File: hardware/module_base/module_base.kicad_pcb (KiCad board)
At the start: 2 copper layers, 100 x 100 mm, 26 parts, among them J1 RJ45_LED_Shielded, J2 Conn_01x24_Female, J3 Conn_01x24_Female, J4 Conn_01x06_Male, Q1 Q_NMOS_GSD, Q2 Q_NMOS_GSD, Q3 Q_NMOS_GSD, Q4 Q_NMOS_GSD, Q5 Q_NMOS_GSD, Q6 Q_NMOS_GSD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

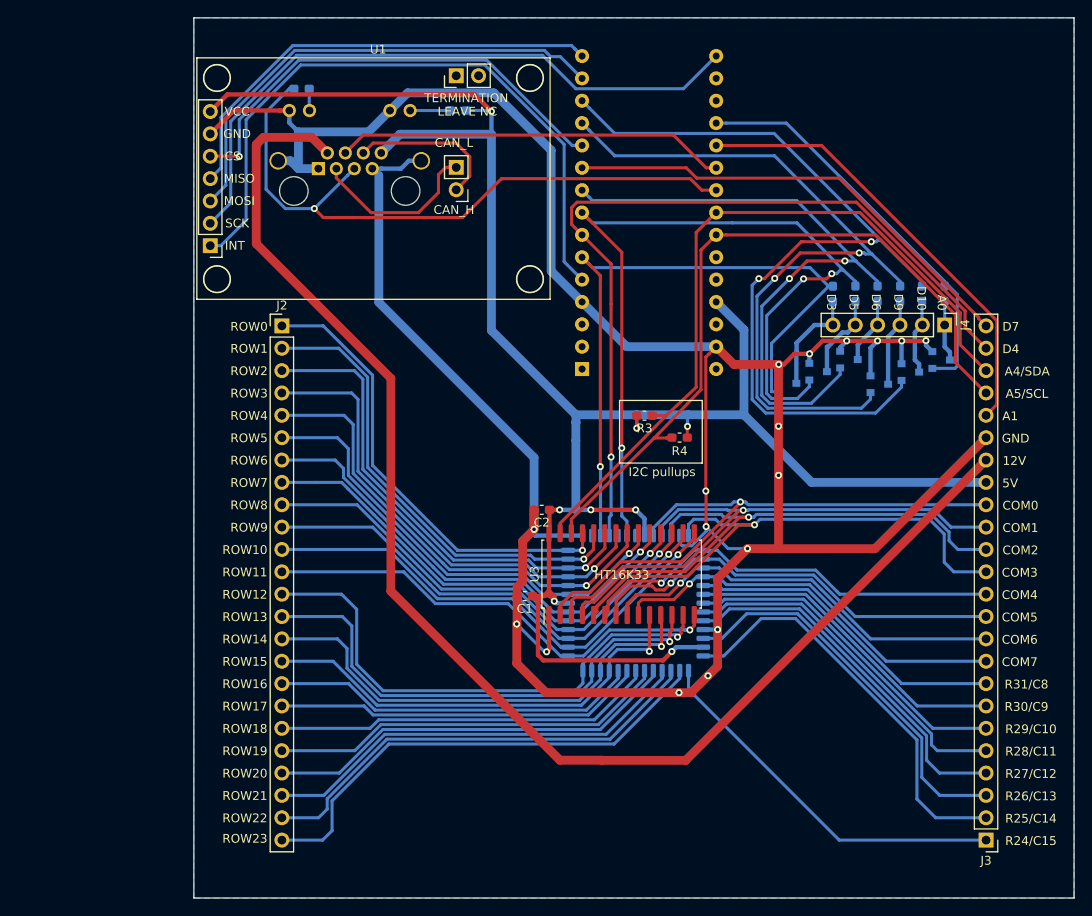
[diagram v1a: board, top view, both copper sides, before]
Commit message: Redo prototyping module layout: CAN module on back, two rows of pins
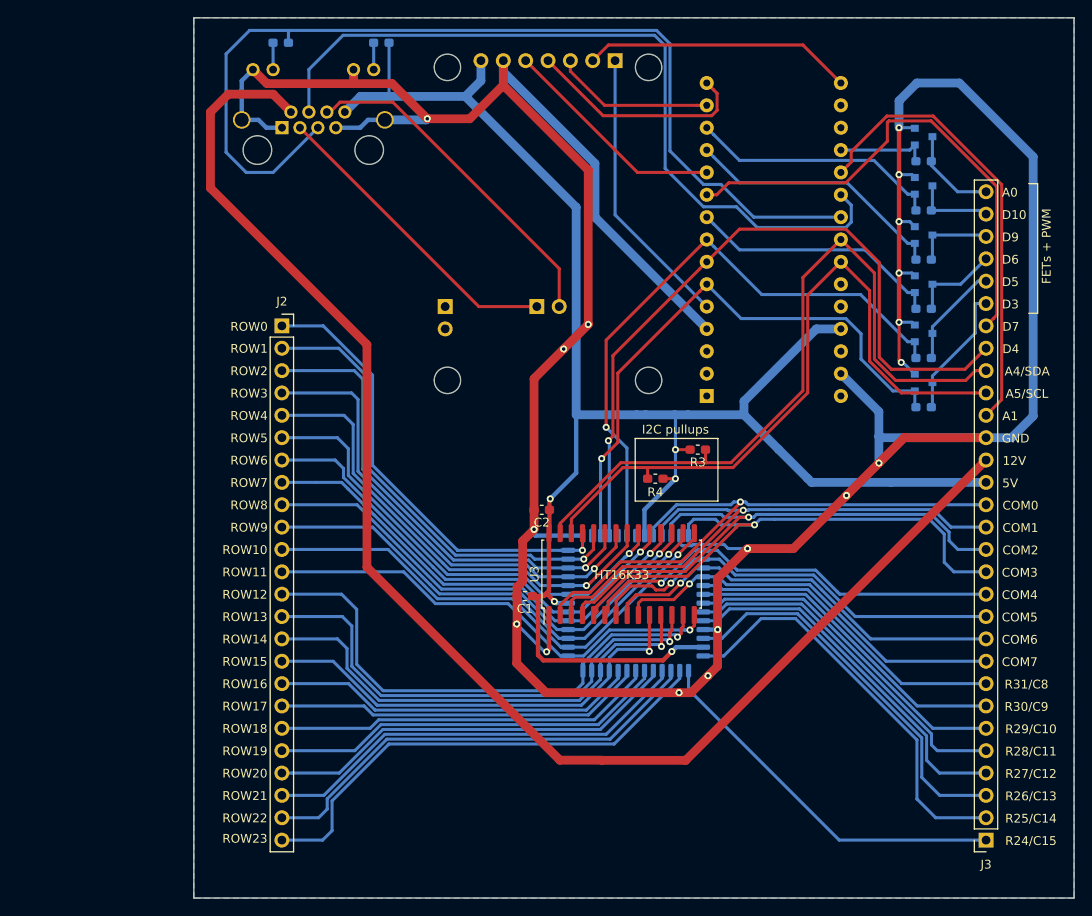
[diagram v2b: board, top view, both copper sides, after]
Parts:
- removed J4: Conn_01x06_Male, Connector_PinHeader_2.54mm:PinHeader_1x06_P2.54mm_Vertical
- J2: footprint Connector_PinHeader_2.54mm:PinHeader_1x24_P2.54mm_Vertical -> Connector_PinSocket_2.54mm:PinSocket_1x24_P2.54mm_Vertical
- J3: value Conn_01x24_Female -> Conn_01x30_Female; footprint Connector_PinHeader_2.54mm:PinHeader_1x24_P2.54mm_Vertical -> Connector_PinSocket_2.54mm:PinSocket_1x30_P2.54mm_Vertical
- U1: moved to B.Cu
- moved Q6 32.0 mm to (152.9, 63.5)
- moved Q5 24.3 mm to (152.9, 69.1)
- moved R10 18.3 mm to (152.9, 66.3), turned to 180 degrees
- moved U1 17.7 mm to (93.5, 63.5), turned to 270 degrees
- moved Q4 16.5 mm to (152.9, 74.7)
- moved A1 14.5 mm to (128.3, 93.0)
- moved R5 13.1 mm to (152.9, 94.2), turned to 180 degrees
- moved Q3 12.4 mm to (152.9, 80.3)
- moved R9 12.2 mm to (152.9, 71.9), turned to 180 degrees
- moved R1 11.6 mm to (91.3, 52.8)
- moved R6 7.30 mm to (152.9, 88.6), turned to 180 degrees
- moved R3 7.18 mm to (127.3, 99.1)
- moved R8 6.51 mm to (152.9, 77.5), turned to 180 degrees
- moved J1 6.22 mm to (80.0, 62.5)
- moved R2 5.74 mm to (79.9, 52.8), turned to 0 degrees
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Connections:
- Q1 pad 1: A0 -> D3
- Q1 pad 3: Net-(J4-Pad1) -> Net-(J3-Pad25)
- Q2 pad 1: D10 -> D5
- Q2 pad 3: Net-(J4-Pad2) -> Net-(J3-Pad26)
- Q3 pad 1: D9 -> D6
- Q3 pad 3: Net-(J4-Pad3) -> Net-(J3-Pad27)
- Q4 pad 1: D6 -> D9
- Q4 pad 3: Net-(J4-Pad4) -> Net-(J3-Pad28)
- Q5 pad 1: D5 -> D10
- Q5 pad 3: Net-(J4-Pad5) -> Net-(J3-Pad29)
- Q6 pad 1: D3 -> A0
- Q6 pad 3: Net-(J4-Pad6) -> Net-(J3-Pad30)
- R10 pad 1: Net-(J4-Pad6) -> Net-(J3-Pad30)
- R10 pad 2: D3 -> A0
- R5 pad 1: Net-(J4-Pad1) -> Net-(J3-Pad25)
- R5 pad 2: A0 -> D3
- R6 pad 1: Net-(J4-Pad2) -> Net-(J3-Pad26)
- R6 pad 2: D10 -> D5
- R7 pad 1: Net-(J4-Pad3) -> Net-(J3-Pad27)
- R7 pad 2: D9 -> D6
- R8 pad 1: Net-(J4-Pad4) -> Net-(J3-Pad28)
- R8 pad 2: D6 -> D9
- R9 pad 1: Net-(J4-Pad5) -> Net-(J3-Pad29)
- R9 pad 2: D5 -> D10
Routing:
- net D10: track 97.0 -> 28.7 mm, vias 2 -> 0
- net D9: track 85.3 -> 29.9 mm, vias 2 -> 0
- net GND: track 344.3 -> 391.1 mm, vias 17 -> 18
- net MODULE_READY: track 44.5 -> 89.1 mm
- net D6: track 72.8 -> 29.1 mm, vias 2 -> 0
- net SCK: track 73.9 -> 30.7 mm
- net Net-(A1-Pad5): track 75.4 -> 32.3 mm
- net MODULE_ENABLE: track 74.3 -> 113.0 mm, vias 1 -> 0
- net MOSI: track 55.0 -> 18.3 mm
- net A0: track 46.8 -> 10.5 mm
- net D5: track 99.7 -> 69.7 mm, vias 3 -> 1
- net Net-(A1-Pad11): track 53.3 -> 25.8 mm, vias 1 -> 0
- net MISO: track 52.3 -> 25.6 mm
- net VCC: track 227.5 -> 204.8 mm, vias 8 -> 5
- net Net-(J1-Pad6): track 17.6 -> 39.0 mm
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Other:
- board text added: "FETs + PWM"

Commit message: ModuleBase PCB: change RJ45 jack, add mounting holes, reorganize
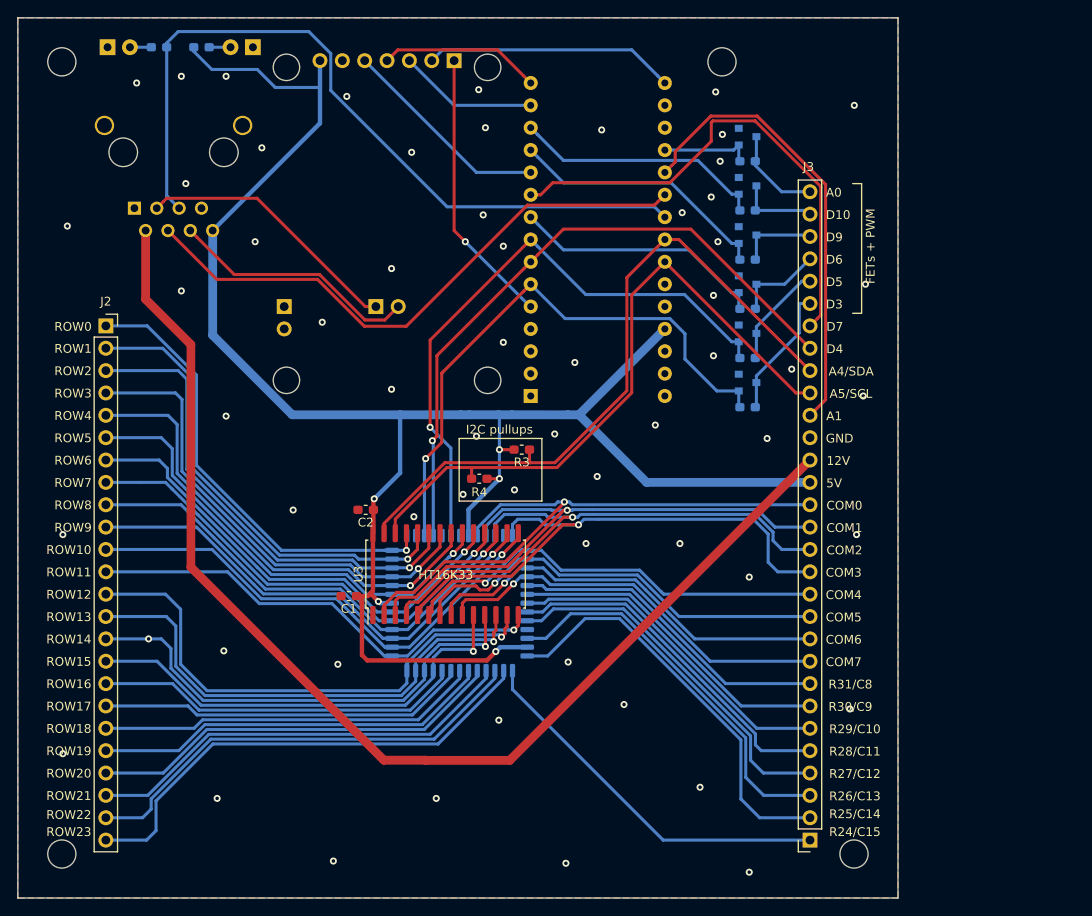
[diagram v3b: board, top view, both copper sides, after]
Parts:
- added D1: LED_Small, LED_THT:LED_D3.0mm, B.Cu at (76.7, 53.3)
- added D2: LED_Small, LED_THT:LED_D3.0mm, B.Cu at (60.2, 53.3)
- added REF**: MountingHole_3.2mm_M3, MountingHole:MountingHole_3.2mm_M3, F.Cu at (55.0, 145.0)
- added REF**: MountingHole_3.2mm_M3, MountingHole:MountingHole_3.2mm_M3, F.Cu at (145.0, 145.0)
- added REF**: MountingHole_3.2mm_M3, MountingHole:MountingHole_3.2mm_M3, F.Cu at (130.0, 55.0)
- added REF**: MountingHole_3.2mm_M3, MountingHole:MountingHole_3.2mm_M3, F.Cu at (55.0, 55.0)
- J1: value RJ45_LED_Shielded -> RJ45_Shielded; footprint Connector_RJ:RJ45_Amphenol_RJHSE538X -> RJ45_5224:RJ45_5224
- moved R1 20.4 mm to (70.9, 53.3), turned to 0 degrees
- moved A1 20.0 mm to (108.3, 93.0)
- moved C1 20.0 mm to (87.6, 115.7)
- moved C2 20.0 mm to (89.5, 105.9)
- moved J2 20.0 mm to (60.0, 85.0)
- moved J3 20.0 mm to (140.0, 143.4)
- moved Q1 20.0 mm to (132.9, 91.4)
- moved Q2 20.0 mm to (132.9, 85.9)
- moved Q3 20.0 mm to (132.9, 80.3)
- moved Q4 20.0 mm to (132.9, 74.7)
- moved Q5 20.0 mm to (132.9, 69.1)
- moved Q6 20.0 mm to (132.9, 63.5)
- moved R10 20.0 mm to (132.9, 66.3)
- moved R3 20.0 mm to (107.3, 99.1)
- moved R4 20.0 mm to (102.4, 102.4)
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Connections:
- R1 pad 2: Net-(J1-Pad12) -> Net-(D1-Pad2)
- R2 pad 1: Net-(J1-Pad10) -> Net-(D2-Pad2)
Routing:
- net GND: track 391.1 -> 0.00 mm, vias 18 -> 60
- net +12V: track 163.5 -> 133.9 mm
- net MODULE_ENABLE: track 113.0 -> 87.7 mm
- net MODULE_READY: track 89.1 -> 67.2 mm
- net Net-(J1-Pad6): track 39.0 -> 28.5 mm
- net VCC: track 204.8 -> 213.7 mm
- net D4: track 82.9 -> 74.6 mm
- net MISO: track 25.6 -> 18.4 mm
- net A4_SDA: track 84.7 -> 78.1 mm
- net Net-(J1-Pad3): track 35.3 -> 30.5 mm
- net A5_SCL: track 79.5 -> 74.8 mm
- net Net-(J1-Pad12): track 3.05 -> 0.00 mm
- net Net-(J1-Pad10): track 3.05 -> 0.00 mm
- net Net-(D2-Pad2): track 0.00 -> 2.43 mm
- net Net-(D1-Pad2): track 0.00 -> 2.43 mm
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- added copper zone on F.Cu, net GND
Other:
- board text added: "Choose FET or resistor for each pin"

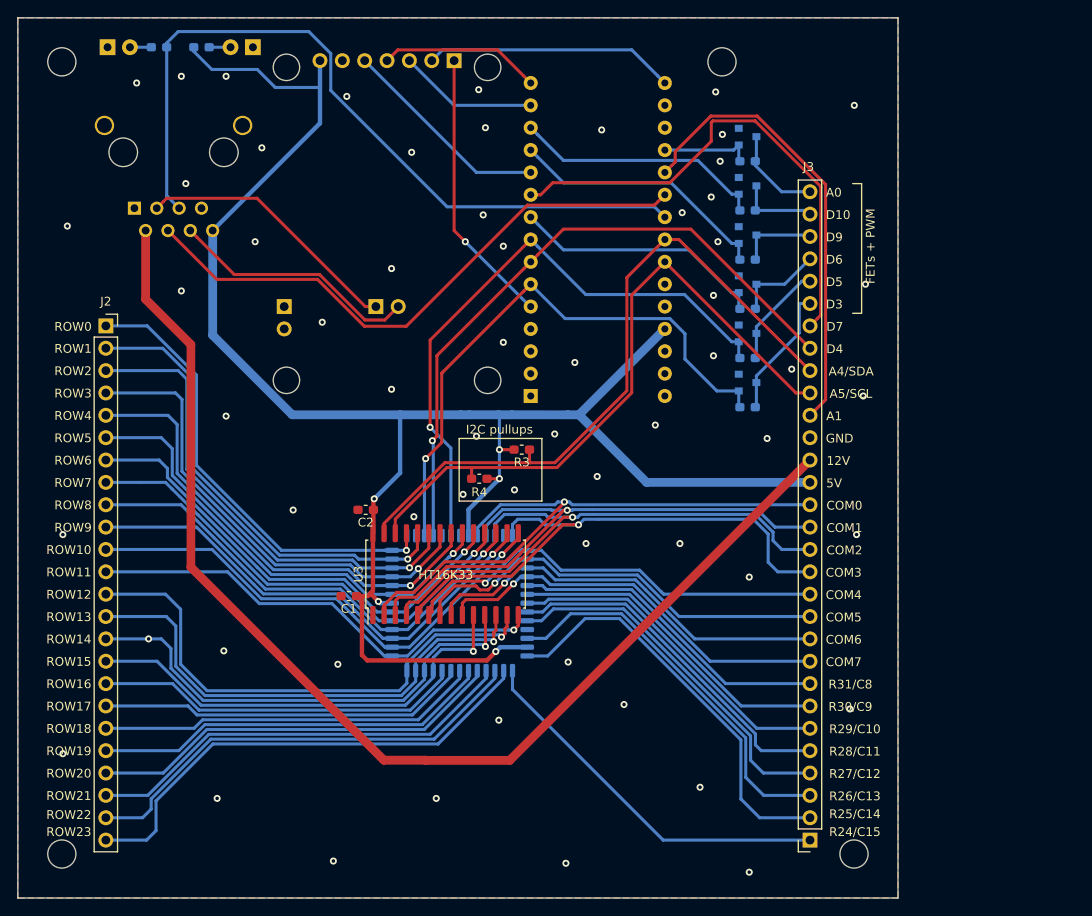
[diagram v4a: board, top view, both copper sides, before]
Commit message: Add identifying silkscreen text, fix missing connections on ModuleBase
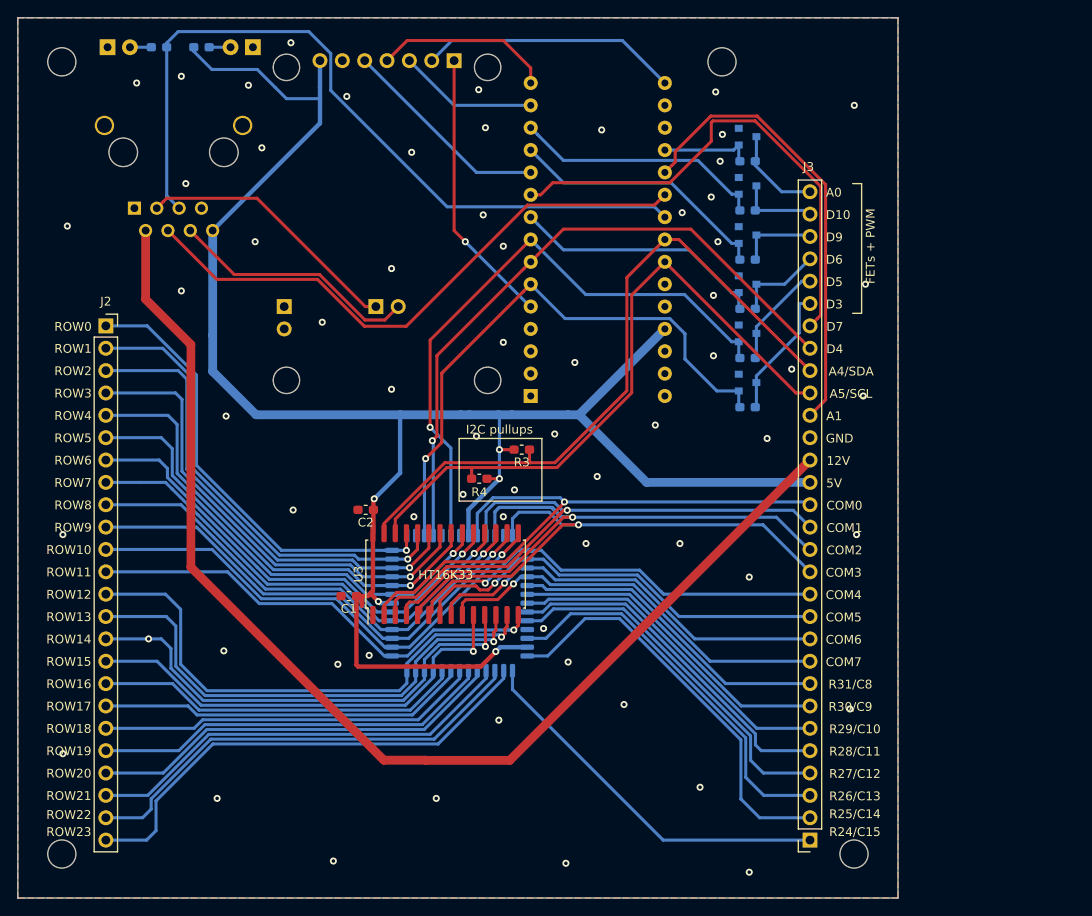
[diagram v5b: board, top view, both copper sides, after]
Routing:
- net COM2: track 64.2 -> 74.3 mm
- net VCC: track 213.7 -> 219.6 mm
- net MISO: track 18.4 -> 20.3 mm
- net COM1: track 65.0 -> 66.5 mm
- net COM0: track 66.5 -> 67.9 mm
- net COM3: track 63.1 -> 61.7 mm
- net SCK: track 28.5 -> 29.4 mm
- net GND: vias 60 -> 64
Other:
- board text added: "BGame Base/Dev Module v1.0 PurkkaKoodari 2020"

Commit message: ModuleBase PCB: add lots of mounting holes and some grounds
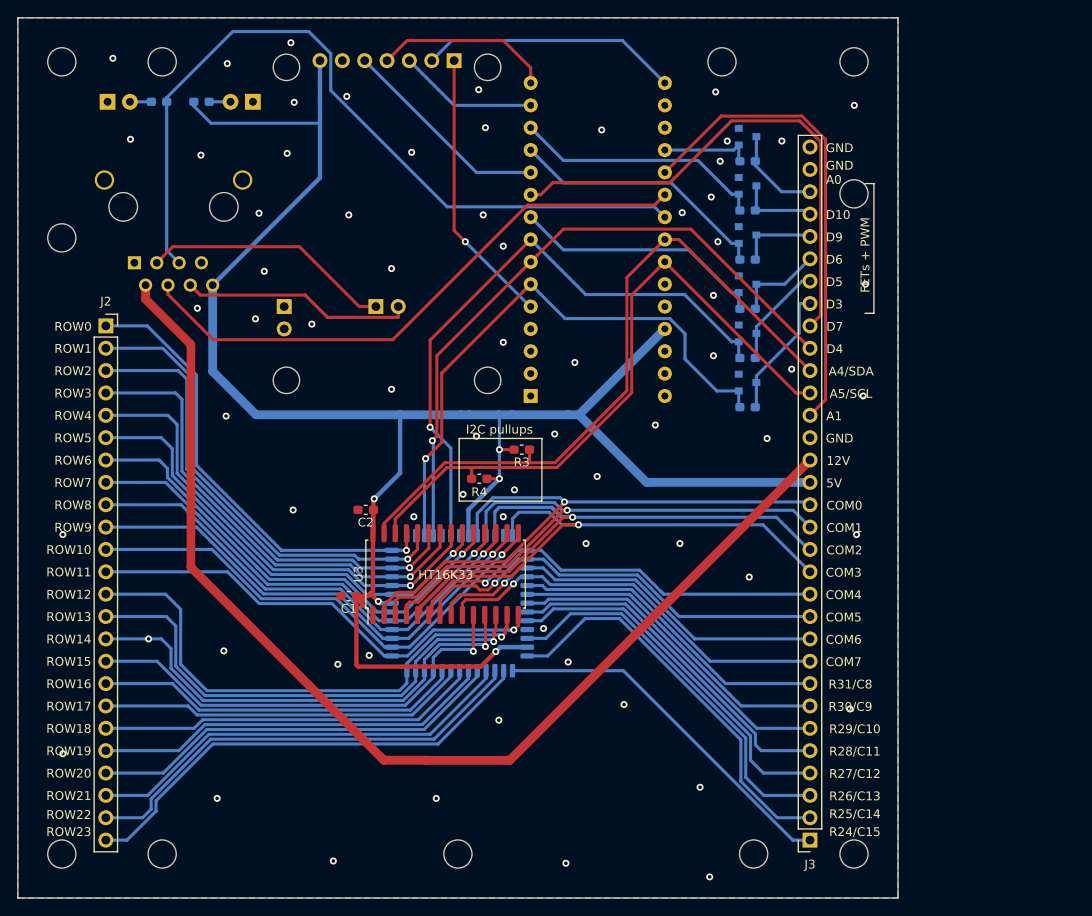
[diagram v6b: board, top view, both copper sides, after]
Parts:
- added REF**: MountingHole_3.2mm_M3, MountingHole:MountingHole_3.2mm_M3, F.Cu at (145.0, 55.0)
- added REF**: MountingHole_3.2mm_M3, MountingHole:MountingHole_3.2mm_M3, F.Cu at (100.0, 145.0)
- added REF**: MountingHole_3.2mm_M3, MountingHole:MountingHole_3.2mm_M3, F.Cu at (145.0, 70.0)
- added REF**: MountingHole_3.2mm_M3, MountingHole:MountingHole_3.2mm_M3, F.Cu at (55.0, 75.0)
- added REF**: MountingHole_3.2mm_M3, MountingHole:MountingHole_3.2mm_M3, F.Cu at (66.4, 55.0)
- added REF**: MountingHole_3.2mm_M3, MountingHole:MountingHole_3.2mm_M3, F.Cu at (133.6, 145.0)
- added REF**: MountingHole_3.2mm_M3, MountingHole:MountingHole_3.2mm_M3, F.Cu at (66.4, 145.0)
- J3: value Conn_01x30_Female -> Conn_01x32_Female; footprint Connector_PinSocket_2.54mm:PinSocket_1x30_P2.54mm_Vertical -> Connector_PinSocket_2.54mm:PinSocket_1x32_P2.54mm_Vertical
- moved J1 6.20 mm to (63.2, 77.8)
- moved D1 6.20 mm to (76.7, 59.5)
- moved D2 6.20 mm to (60.2, 59.5)
- moved R1 6.20 mm to (70.9, 59.5)
- moved R2 6.20 mm to (66.0, 59.5)
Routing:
- net +12V: track 133.9 -> 127.7 mm
- net MODULE_ENABLE: track 87.7 -> 90.2 mm
- net A1: track 51.8 -> 54.1 mm
- net Net-(J1-Pad6): track 28.5 -> 26.4 mm
- net Net-(J1-Pad3): track 30.5 -> 28.5 mm
- net D7: track 57.1 -> 58.8 mm
- net VCC: track 219.6 -> 218.2 mm
- net Net-(J2-Pad24): track 55.7 -> 54.4 mm
- net Net-(J3-Pad1): track 43.0 -> 41.8 mm
- net Net-(J3-Pad2): track 47.2 -> 46.0 mm
- net MODULE_READY: track 67.2 -> 66.5 mm
- net GND: vias 64 -> 68
